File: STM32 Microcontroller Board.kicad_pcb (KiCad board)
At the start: 4 copper layers, 177 parts, among them J1 F407 SWD, J10 USB_B_Micro, J2 GPIO, J3 Conn_01x02_Pin, J4 F103 SWD, J5 USB_B_Micro, J6 Ethernet, J7 12V IN, J8 12V RGB LED, J9 Relay IO, Q1 PMOS, Q2 NMOS, Q3 NMOS, Q4 NMOS, SW1 SW_Push, SW2 SW_Push, SW3 SW_Push, SW4 SW_Push, SW5 SW_Push, SW6 SW_Push, U1 STM32F407VGTx, U2 MCP1825S-3302E/EB, U3 STM32F103C8T6, U4 USBLC6-2SC6, U5 DP83826IRHBR, U6 TLV9001TIDCKR, U7 ULN2803CDWR, U8 USBLC6-2SC6, Y1 8MHz, Y2 25MHz

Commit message: Layout placement
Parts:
- C1, C11, C12, C13, C14, C2, C20, C21, C22, C23, C24, C26, C27, C28, C29, C3, C30, C34, C39, C4, C40, C41, C42, C43, C46, C47, C5, C6, C7, C8, C9, D13, D7, D8, F1, F3, R15, R16, R17, R18, R25, R29, R3, R33, R38, R4, R40, R44, R45, R48, R50, R51, R52, R55, R56, R57, R58, R59, R6, R60, R61, R62, R7, R8: moved to B.Cu
- D11: value SMBJ15A -> SMBJ15CA; moved to B.Cu
- moved J3 168.0 mm to (113.2, 88.9), turned to 180 degrees
- moved D1 161.3 mm to (113.1, 81.8), turned to 90 degrees
- moved U2 160.2 mm to (122.4, 90.2), turned to 180 degrees
- moved C19 158.0 mm to (117.0, 81.4), turned to 180 degrees
- moved TP4 156.8 mm to (113.2, 94.9)
- moved R10 156.6 mm to (113.3, 78.5), turned to 180 degrees
- moved C18 153.8 mm to (116.9, 79.6), turned to 180 degrees
- moved C16 147.5 mm to (128.0, 80.0)
- moved C15 143.5 mm to (128.1, 81.6)
- moved SW1 134.3 mm to (128.8, 100.4)
- moved J1 129.0 mm to (132.5, 80.9)
- moved R26 125.4 mm to (137.8, 51.0)
- moved R23 124.0 mm to (140.2, 51.9), turned to -90 degrees
- moved R27 123.4 mm to (138.6, 46.7)
- moved Q2 123.3 mm to (155.6, 130.2), turned to 180 degrees
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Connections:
- D11 pad 1: +12V -> GND
- D11 pad 2: GND -> Net-(D11-A2)
- F2 pad 1: Net-(F2-Pad1) -> Net-(D11-A2)
- J2 pad 10: GND -> /Main MCU/PA3
- J2 pad 11: +5V -> /Main MCU/PA5
- J2 pad 12: +3.3V -> /Main MCU/PB1
- J2 pad 13: /Main MCU/RESET -> /Main MCU/PB5
- J2 pad 14: /Main MCU/PA3 -> /Main MCU/PE14
- J2 pad 15: /Main MCU/PB1 -> /Main MCU/PA6
- J2 pad 16: /Main MCU/PE14 -> /Main MCU/PD15
- J2 pad 17: /Main MCU/PD15 -> /Main MCU/PA0
- J2 pad 2: +5V -> GND
- J2 pad 3: +3.3V -> +5V
- J2 pad 4: /Main MCU/PA8 -> +5V
- J2 pad 5: /Main MCU/PC9 -> +3.3V
- J2 pad 6: /Main MCU/PA5 -> +3.3V
- J2 pad 7: /Main MCU/PB5 -> /Main MCU/PA8
- J2 pad 8: /Main MCU/PA6 -> /Main MCU/RESET
- J2 pad 9: /Main MCU/PA0 -> /Main MCU/PC9
- J7 pad 1: Net-(F2-Pad1) -> Net-(D11-A2)
- J8 pad 1: +12V -> /LED Driver/R_LED
- J8 pad 2: /LED Driver/R_LED -> /LED Driver/G_LED
- J8 pad 3: /LED Driver/G_LED -> /LED Driver/B_LED
- J8 pad 4: /LED Driver/B_LED -> +12V
- J9 pad 2: /AC PWR ctrl & USB FS/CH1 -> GND
- J9 pad 3: /AC PWR ctrl & USB FS/CH2 -> /AC PWR ctrl & USB FS/CH1
- J9 pad 4: /AC PWR ctrl & USB FS/CH3 -> /AC PWR ctrl & USB FS/CH5
- J9 pad 5: /AC PWR ctrl & USB FS/CH4 -> /AC PWR ctrl & USB FS/CH2
- J9 pad 6: GND -> /AC PWR ctrl & USB FS/CH6
- J9 pad 7: /AC PWR ctrl & USB FS/CH5 -> /AC PWR ctrl & USB FS/CH3
- J9 pad 8: /AC PWR ctrl & USB FS/CH6 -> /AC PWR ctrl & USB FS/CH7
- J9 pad 9: /AC PWR ctrl & USB FS/CH7 -> /AC PWR ctrl & USB FS/CH4
- U1 pad 86: unconnected-(U1-PD5-Pad86) -> /Debugger/TX
- U1 pad 87: unconnected-(U1-PD6-Pad87) -> /Debugger/RX
- U3 pad 12: unconnected-(U3-PA2-Pad12) -> /Debugger/TX
- U3 pad 13: unconnected-(U3-PA3-Pad13) -> /Debugger/RX
- U3 pad 25: /Main MCU/T_SWDIO -> unconnected-(U3-PB12-Pad25)
- U3 pad 27: unconnected-(U3-PB14-Pad27) -> /Main MCU/T_SWDIO
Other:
- board outline added: 69.1 x 94.3 mm
- board text added: "12V"
- board text added: "12VDC"
- board text added: "3.3V"
- board text added: "5V"
- board text added: "BOOT"
- board text added: "CH1"
- board text added: "CH2"
- board text added: "CH3"
- board text added: "CH4"
- board text added: "CH5"
- board text added: "CH6"
- board text added: "CH7"
- board text added: "CH8"
- board text added: "CLK"
- board text added: "DIO"
- board text added: "F103_SWD"
- board text added: "GND"
- board text added: "PA0"
- board text added: "PA3"
- board text added: "PA5"
- board text added: "PA6"
- board text added: "PA8"
- board text added: "PB1"
- board text added: "PB5"
- board text added: "PC11"
- board text added: "PC9"
- board text added: "PD15"
- board text added: "PE14"
- board text added: "RESET"
- board text added: "RST"
- board text added: "S1"
- board text added: "S2"
- board text added: "STM_RST"
- board text added: "SWO"
- board text added: "TRACE"

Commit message: Layout Routing
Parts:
- removed TP9: D-, TestPoint:TestPoint_Pad_D1.0mm
- added C17: 0.1uF, Capacitor_SMD:C_0402_1005Metric, F.Cu at (135.6, 90.7)
- added D1: 3.3V, Diode_SMD:D_SOD-323F, F.Cu at (134.9, 89.1)
- added G***: LOGO, LOGO, F.Cu at (156.3, 55.7)
- added H1: MountingHole, MountingHole:MountingHole_3.2mm_M3_Pad, F.Cu at (107.6, 48.9)
- added H2: MountingHole, MountingHole:MountingHole_3.2mm_M3_Pad, F.Cu at (169.5, 48.9)
- added H3: MountingHole, MountingHole:MountingHole_3.2mm_M3_Pad, F.Cu at (169.4, 134.3)
- added H4: MountingHole, MountingHole:MountingHole_3.2mm_M3_Pad, F.Cu at (107.6, 134.3)
- added R44: 100k, Resistor_SMD:R_0603_1608Metric, B.Cu at (138.9, 103.5)
- added R45: 22.1k, Resistor_SMD:R_0603_1608Metric, B.Cu at (139.8, 101.2)
- C10, FB1: moved to B.Cu
- C11, C2, R8: moved to F.Cu
- C21: renamed from C20; moved to F.Cu
- C26: renamed from C25; moved to B.Cu
- C31: renamed from C30; moved to F.Cu
- C6: value 0.1uF -> 1uF; footprint Capacitor_SMD:C_0402_1005Metric -> Capacitor_SMD:C_0603_1608Metric
- C7: value 1uF -> 0.1uF; footprint Capacitor_SMD:C_0603_1608Metric -> Capacitor_SMD:C_0402_1005Metric
- R10: renamed from R11; moved to B.Cu
- R11: renamed from R12; moved to B.Cu
- R12: renamed from R13; moved to B.Cu
- R13: renamed from R14; moved to B.Cu
- TP8: value D+ -> 5V; footprint TestPoint:TestPoint_Pad_D1.0mm -> TestPoint:TestPoint_Keystone_5000-5004_Miniature
- U4, U8: value USBLC6-2SC6 -> USBLC6-2
- moved SW2 64.4 mm to (132.4, 104.0)
- moved SW5 49.1 mm to (130.6, 72.5), turned to 90 degrees
- moved TP2 28.4 mm to (146.7, 78.6), turned to 90 degrees
- moved C11 24.9 mm to (135.9, 97.3), turned to 180 degrees
- moved SW6 24.8 mm to (106.9, 72.5), turned to 90 degrees
- moved TP5 23.7 mm to (138.4, 80.2)
- moved R67 22.4 mm to (167.3, 108.8)
- moved D13 22.4 mm to (167.4, 107.0)
- moved R65 22.3 mm to (156.1, 100.2)
- moved J10 21.7 mm to (172.2, 102.4)
- moved R66 21.6 mm to (156.1, 101.7)
- moved R68 21.4 mm to (168.7, 99.2)
- moved U8 21.4 mm to (167.4, 102.7)
- moved D14 20.9 mm to (165.7, 100.0)
- moved TP8 20.7 mm to (161.4, 98.6)
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- renumbered C17 to C18, C18 to C19, C19 to C20, C21 to C22, C22 to C23, C23 to C24, C24 to C25, C26 to C27, C27 to C28, C28 to C29, C29 to C30, C31 to C32, C32 to C33, C33 to C34, C34 to C35, C35 to C36, C38 to C37, C36 to C38, C37 to C39, C39 to C40, C40 to C41, C41 to C42, C42 to C43, C43 to C44, C44 to C45, C45 to C47, C47 to C48, C48 to C49, C49 to C50, C50 to C51, C51 to C52, C52 to C53, C53 to C54, D8 to D10, D10 to D11, D11 to D12, D12 to D13, D13 to D14, D1 to D2, D2 to D3, D3 to D4, D4 to D5, D5 to D6, D6 to D7, D7 to D8, R10 to R14, R44 to R46, R45 to R47, R46 to R48, R47 to R49, R48 to R50, R49 to R51, R50 to R52, R51 to R53, R52 to R54, R53 to R55, R54 to R56, R55 to R57, R56 to R58, R57 to R59, R58 to R60, R59 to R61, R60 to R62, R61 to R63, R62 to R64, R64 to R65, R65 to R66, R63 to R67, R66 to R68
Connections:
- net /Debugger/USB_DN renamed /Debugger/USB_N
- net /Debugger/USB_DP renamed /Debugger/USB_P
- net Net-(R64-Pad1) renamed /AC PWR ctrl & USB FS/USB_FS_DP
- net Net-(R65-Pad2) renamed /AC PWR ctrl & USB FS/USB_FS_DN
- C6 pad 1: +3.3V -> Net-(U1-VDDA)
- C7 pad 1: Net-(U1-VDDA) -> +3.3V
- C8 pad 1: +3.3V -> Net-(U1-VDDA)
- C9 pad 1: Net-(U1-VDDA) -> +3.3V
- D10 pad 1: /Ethernet PHY/RD_N -> /Ethernet PHY/TD_P
- D10 pad 2: /Ethernet PHY/RD_P -> /Ethernet PHY/TD_N
- D10 pad 4: /Ethernet PHY/TD_N -> /Ethernet PHY/RD_P
- D10 pad 5: /Ethernet PHY/TD_P -> /Ethernet PHY/RD_N
- D8 pad 2: Net-(D7-A) -> Net-(D8-A)
- F1 pad 1: Net-(D7-A) -> Net-(D8-A)
- J2 pad 12: /Main MCU/PB1 -> /Main MCU/PC8
- TP8 pad 1: /AC PWR ctrl & USB FS/USB_OTG_FS_DP -> +5V
- U1 pad 65: unconnected-(U1-PC8-Pad65) -> /Main MCU/PC8
- U4 pad 5: Net-(D7-A) -> Net-(J5-VBUS)
- U8 pad 5: /AC PWR ctrl & USB FS/USB_OTG_FS_VBUS -> Net-(J10-VBUS)
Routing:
- net +5V: track 0.00 -> 153.5 mm, vias 0 -> 2
- net GND: track 0.00 -> 108.0 mm, vias 0 -> 57
- net /Main MCU/T_SWDIO: track 0.00 -> 96.6 mm, vias 0 -> 2
- net /Main MCU/T_SWCLK: track 0.00 -> 92.3 mm, vias 0 -> 3
- net /Main MCU/T_SWO: track 0.00 -> 88.0 mm, vias 0 -> 4
- net /Debugger/STM_RST: track 0.00 -> 57.2 mm, vias 0 -> 3
- net +3.3V: track 0.00 -> 56.8 mm, vias 0 -> 30
- net /Main MCU/RESET: track 0.00 -> 55.9 mm, vias 0 -> 2
- net /Main MCU/PA6: track 0.00 -> 53.5 mm, vias 0 -> 2
- net /Ethernet PHY/MDC: track 0.00 -> 52.5 mm, vias 0 -> 2
- net /Ethernet PHY/PHY_RST: track 0.00 -> 46.6 mm, vias 0 -> 2
- net /Ethernet PHY/TX_D0: track 0.00 -> 40.8 mm, vias 0 -> 2
- net /Ethernet PHY/MDIO: track 0.00 -> 40.7 mm, vias 0 -> 3
- net /Ethernet PHY/CRS_DV: track 0.00 -> 38.9 mm, vias 0 -> 2
- net /Ethernet PHY/TX_D1: track 0.00 -> 38.8 mm, vias 0 -> 2
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- added copper zone on B.Cu, net +3.3V
- added copper zone on F.Cu, net +3.3V
- added copper zone on In2.Cu, net +3.3V
- added copper zone on F.Cu, net +5V
- added copper zone on F.Cu, net /Main MCU/PA9
- added copper zone on B.Cu, net GND
- added copper zone on F.Cu, net GND
- added copper zone on In1.Cu, net GND
- added copper zone on F.Cu, net Net-(J3-Pin_2)
- added copper zone on B.Cu, net Net-(U1-VDDA)
- added copper zone on B.Cu, net Net-(U5-VDDA3V3)
- added copper zone on F.Cu, net Net-(U5-VDDA3V3)
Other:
- board size 69.1 x 94.3 mm -> 74.8 x 98.3 mm
- board text added: "3V3"
- board text added: "DESKNODE-F4"
- board text added: "ETH_RST"
- board text added: "Rev.1.0 06/2026"
- board text added: "_electronic_projects"

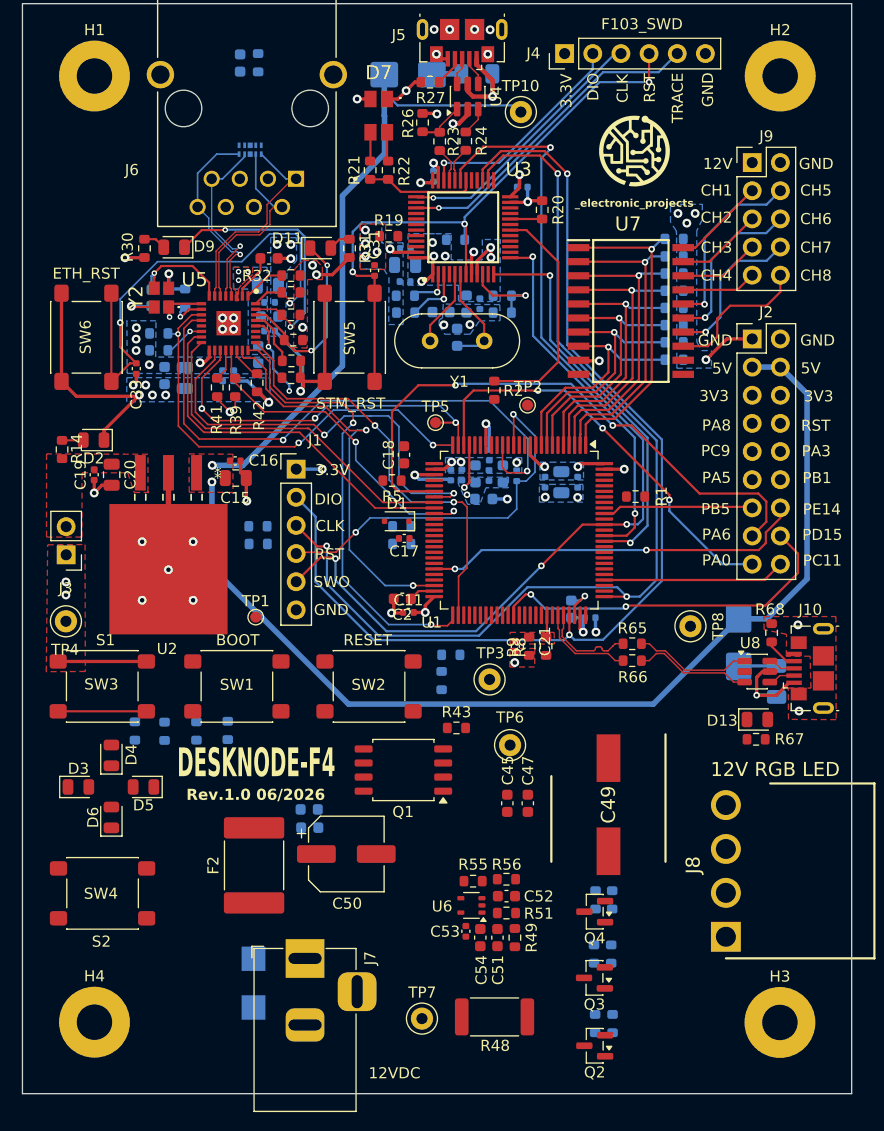
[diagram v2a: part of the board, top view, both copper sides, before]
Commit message: Layout - 12V Power path
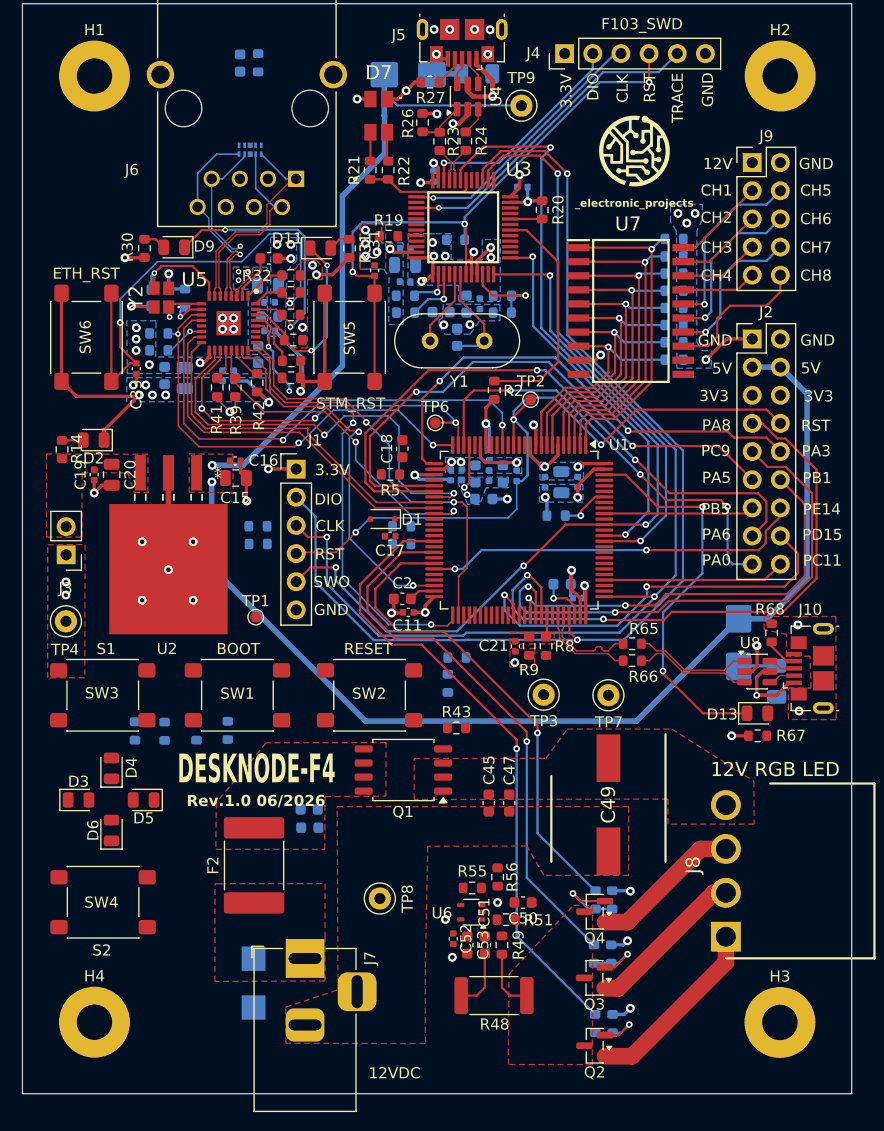
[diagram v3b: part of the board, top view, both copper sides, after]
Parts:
- removed C54: 1uF, Capacitor_SMD:C_0603_1608Metric
- removed TP10: 5V, TestPoint:TestPoint_Keystone_5000-5004_Miniature
- removed TP5: RMII_REF_CLK, TestPoint:TestPoint_Pad_D1.0mm
- added TP9: 5V, TestPoint:TestPoint_Keystone_5000-5004_Miniature, F.Cu at (146.1, 51.6)
- C50: value 100uF -> 0.47uF; footprint Capacitor_SMD:CP_Elec_6.3x7.7 -> Capacitor_SMD:C_0603_1608Metric
- C52: value 0.47uF -> 0.1uF; footprint Capacitor_SMD:C_0603_1608Metric -> Capacitor_SMD:C_0402_1005Metric
- C53: value 0.1uF -> 1uF; footprint Capacitor_SMD:C_0402_1005Metric -> Capacitor_SMD:C_0603_1608Metric
- R1: moved to B.Cu
- TP6: value 12V -> RMII_REF_CLK; footprint TestPoint:TestPoint_Keystone_5000-5004_Miniature -> TestPoint:TestPoint_Pad_D1.0mm
- TP7: value GND -> 12V
- TP8: value 5V -> GND
- moved TP8 37.3 mm to (133.3, 123.1)
- moved TP7 33.7 mm to (154.0, 104.8)
- moved TP6 29.8 mm to (138.3, 80.2)
- moved C50 16.5 mm to (146.3, 123.5), turned to 180 degrees
- moved R1 7.38 mm to (149.3, 88.6), turned to 180 degrees
- moved C52 6.15 mm to (140.0, 126.8), turned to -90 degrees
- moved TP3 5.07 mm to (148.1, 104.7)
- moved C5 2.40 mm to (149.8, 94.8), turned to 0 degrees
- moved C9 2.08 mm to (151.2, 96.0)
- moved R48 1.93 mm to (143.7, 131.9)
- moved C45 1.68 mm to (143.2, 114.5)
- moved C47 1.68 mm to (145.0, 114.5)
- moved R49 1.35 mm to (144.4, 127.3)
- moved C51 1.32 mm to (142.8, 127.3), turned to 90 degrees
- moved C17 1.29 mm to (134.3, 90.5)
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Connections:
- C50 pad 1: +12V -> Net-(C50-Pad1)
- C51 pad 1: Net-(C51-Pad1) -> GND
- C51 pad 2: GND -> Net-(U6-+)
- C52 pad 1: GND -> +3.3V
- C52 pad 2: Net-(U6-+) -> GND
- Q1 pad 1: Net-(Q1-D) -> +12V
- Q1 pad 2: Net-(Q1-G) -> +12V
- Q1 pad 4: (no net) -> Net-(Q1-G)
- Q1 pad 5: (no net) -> Net-(Q1-D)
- Q1 pad 6: (no net) -> Net-(Q1-D)
- Q1 pad 7: (no net) -> Net-(Q1-D)
- Q1 pad 8: (no net) -> Net-(Q1-D)
- R49 pad 2: Net-(C51-Pad1) -> Net-(C50-Pad1)
- R51 pad 1: Net-(C51-Pad1) -> Net-(C50-Pad1)
- TP6 pad 1: +12V -> /Ethernet PHY/REF_CLK
- TP7 pad 1: GND -> +12V
- TP8 pad 1: +5V -> GND
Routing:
- net /LED Driver/R_PWM: track 0.00 -> 57.5 mm, vias 0 -> 1
- net /Main MCU/PA8: track 0.00 -> 54.5 mm, vias 0 -> 2
- net /Main MCU/PA5: track 0.00 -> 51.8 mm, vias 0 -> 2
- net /LED Driver/G_PWM: track 0.00 -> 50.1 mm, vias 0 -> 1
- net /Main MCU/PC9: track 0.00 -> 47.6 mm, vias 0 -> 2
- net /Main MCU/PA3: track 0.00 -> 44.7 mm, vias 0 -> 2
- net /LED Driver/B_PWM: track 0.00 -> 44.1 mm, vias 0 -> 1
- net /Main MCU/PC8: track 0.00 -> 37.6 mm, vias 0 -> 2
- net /AC PWR ctrl & USB FS/LED_USB_n: track 0.00 -> 35.6 mm, vias 0 -> 2
- net /Main MCU/RESET: track 55.9 -> 87.2 mm, vias 2 -> 3
- net GND: track 108.0 -> 135.5 mm, vias 57 -> 63
- net /LED Driver/R_LED: track 0.00 -> 16.7 mm
- net /LED Driver/G_LED: track 0.00 -> 14.5 mm
- net /LED Driver/B_LED: track 0.00 -> 13.6 mm
- net Net-(R3-Pad2): track 7.96 -> 0.00 mm
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- added copper zone on F.Cu, net +12V
- added copper zone on F.Cu, net Net-(D12-A2)
- added copper zone on F.Cu, net Net-(Q1-D)
- added copper zone on F.Cu, net Net-(Q2-S)

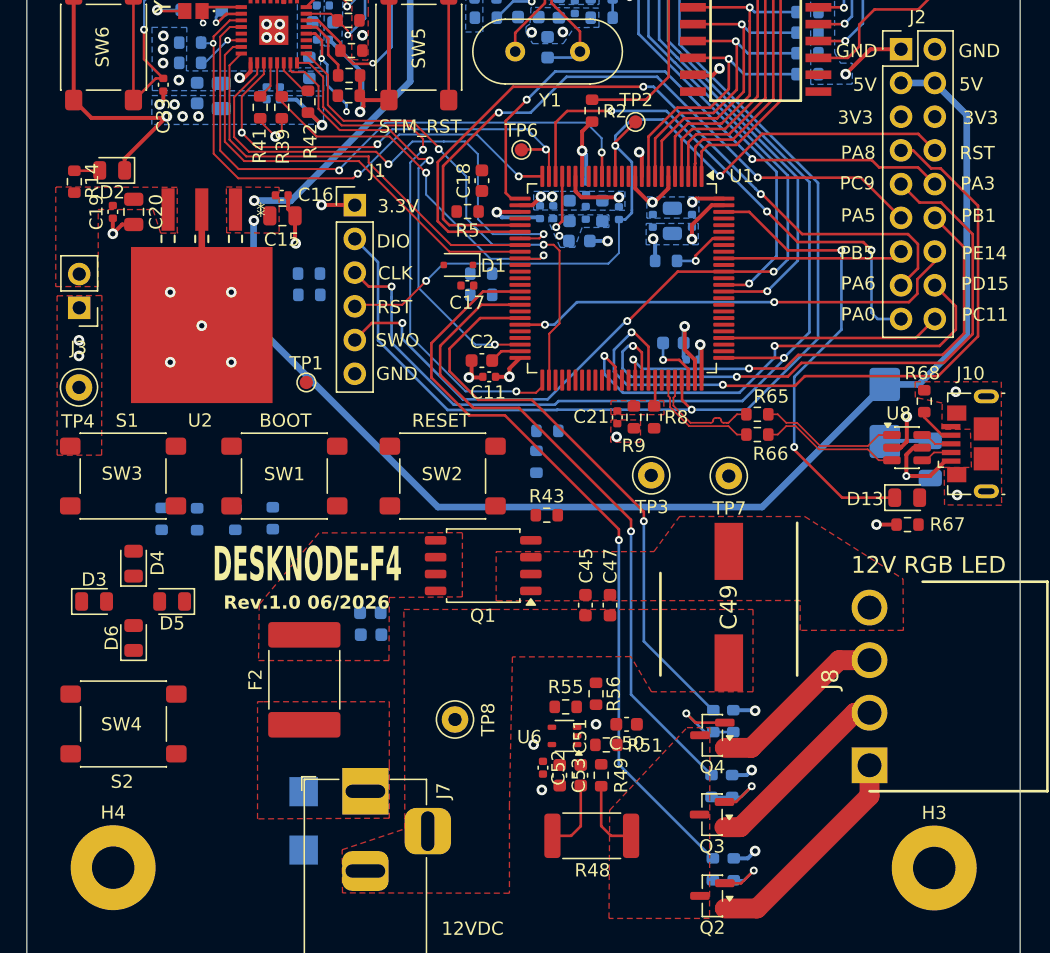
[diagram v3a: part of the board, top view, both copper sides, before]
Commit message: Updated layout
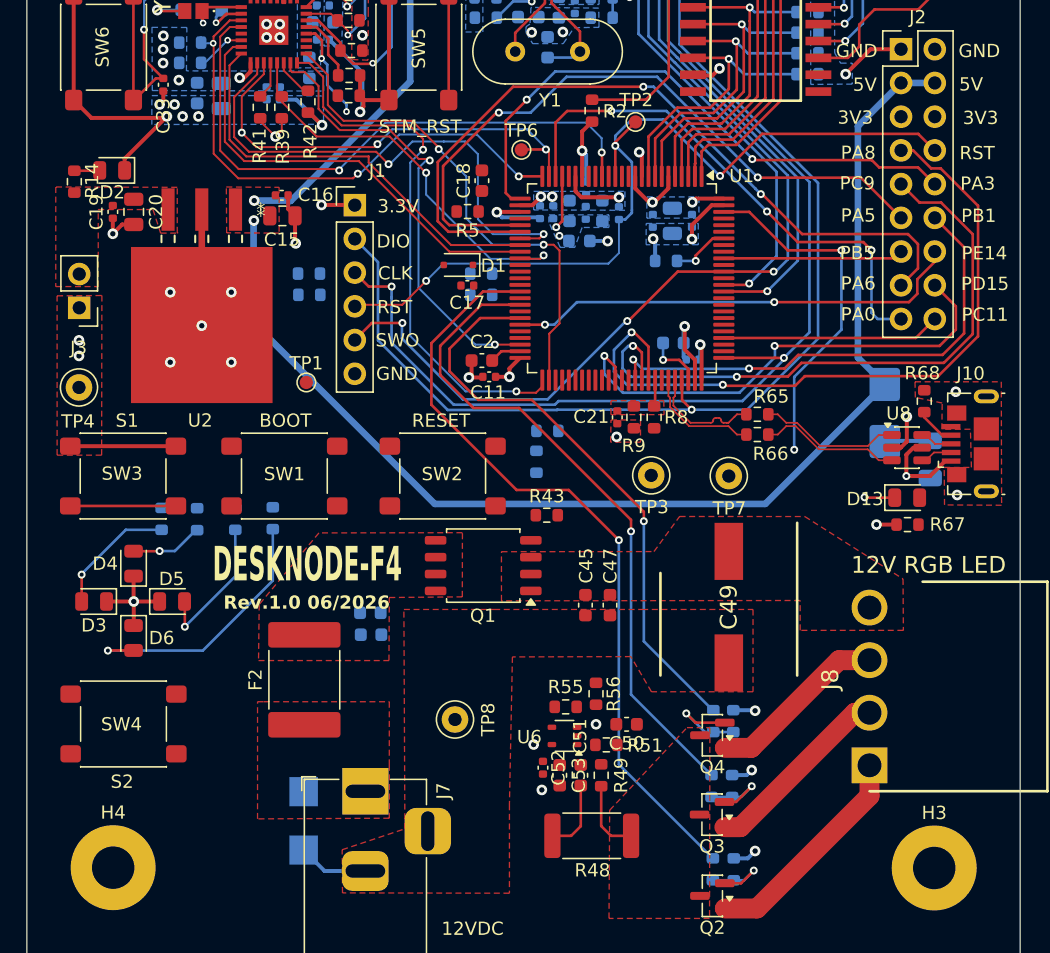
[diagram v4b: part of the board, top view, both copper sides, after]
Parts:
- turned D3 to 180 degrees
- turned D5 to 0 degrees
- turned D6 to -90 degrees
- turned R10 to -90 degrees
- turned R11 to -90 degrees
- turned R12 to -90 degrees
- turned R13 to -90 degrees
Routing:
- net Net-(D6-A): track 0.00 -> 20.4 mm, vias 0 -> 1
- net GND: track 135.5 -> 148.5 mm, vias 63 -> 64
- net Net-(D5-A): track 0.00 -> 10.8 mm, vias 0 -> 1
- net Net-(D3-A): track 0.00 -> 9.48 mm, vias 0 -> 1
- net Net-(R3-Pad2): track 0.00 -> 7.96 mm
- net +3.3V: track 58.2 -> 66.1 mm
- net /AC PWR ctrl & USB FS/LED_USB_n: track 35.6 -> 28.8 mm, vias 2 -> 3
- net Net-(D4-A): track 0.00 -> 5.45 mm, vias 0 -> 1
- net +5V: track 152.3 -> 149.2 mm
- net /LED Driver/R_PWM: track 57.5 -> 58.2 mm
